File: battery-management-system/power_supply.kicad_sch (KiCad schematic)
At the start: 21 parts, among them U1 L6982C33DR, U2 L6982C33DR

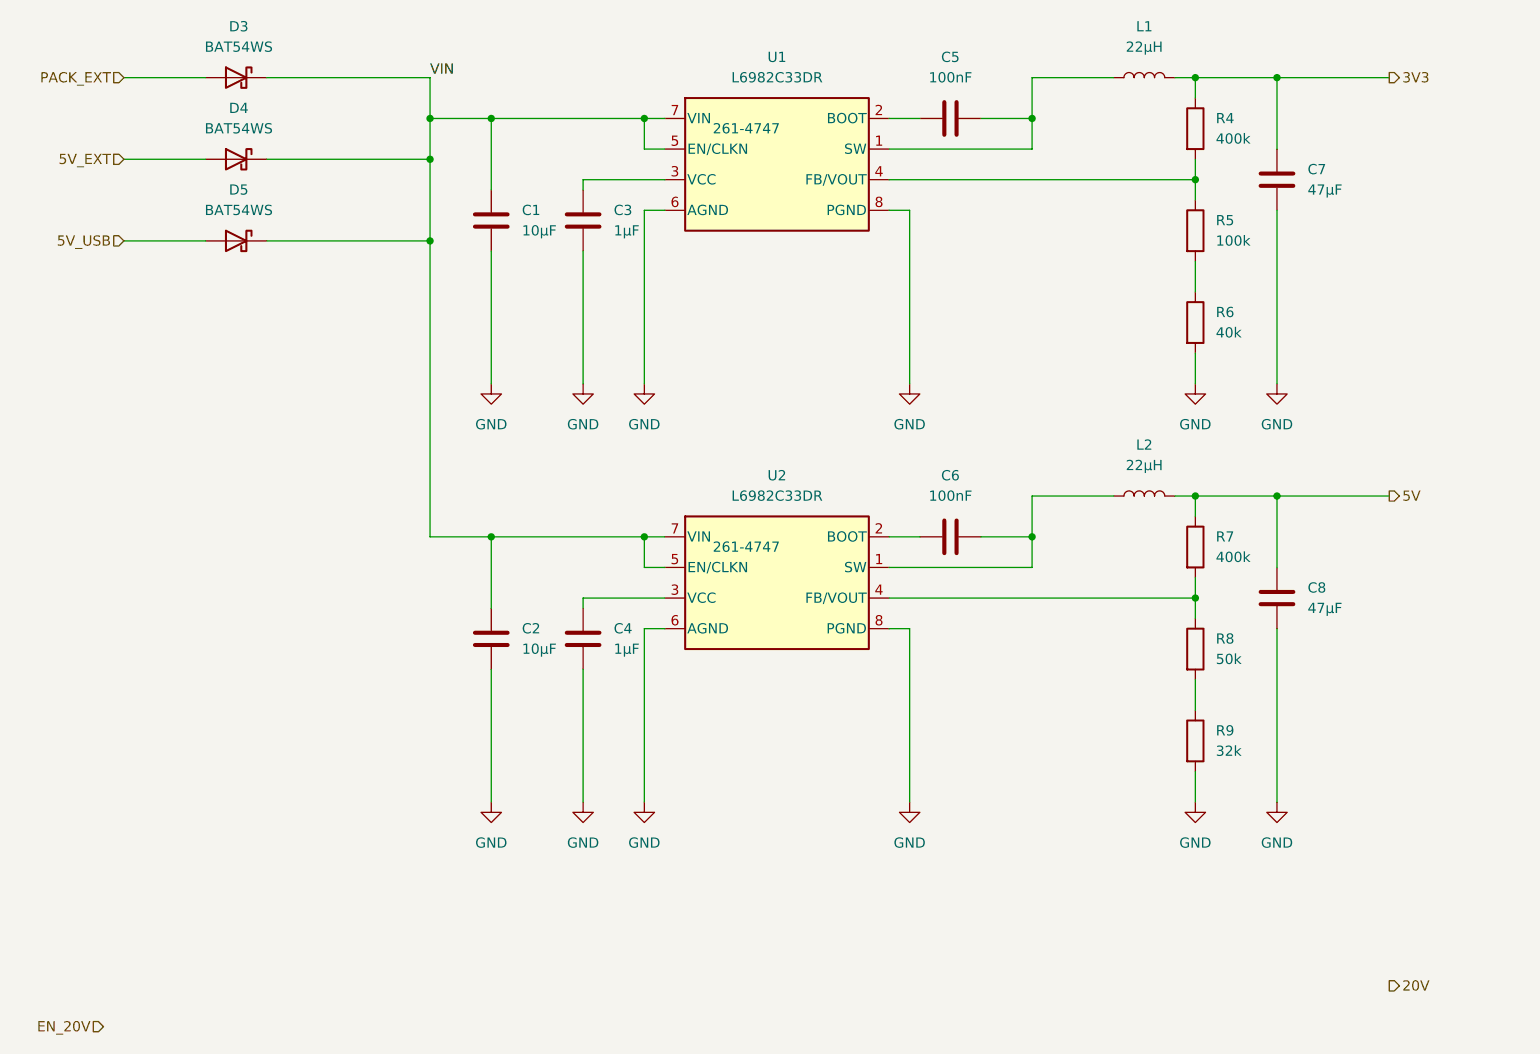
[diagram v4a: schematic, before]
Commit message: specify footprints for resistors, capacitors and inductances
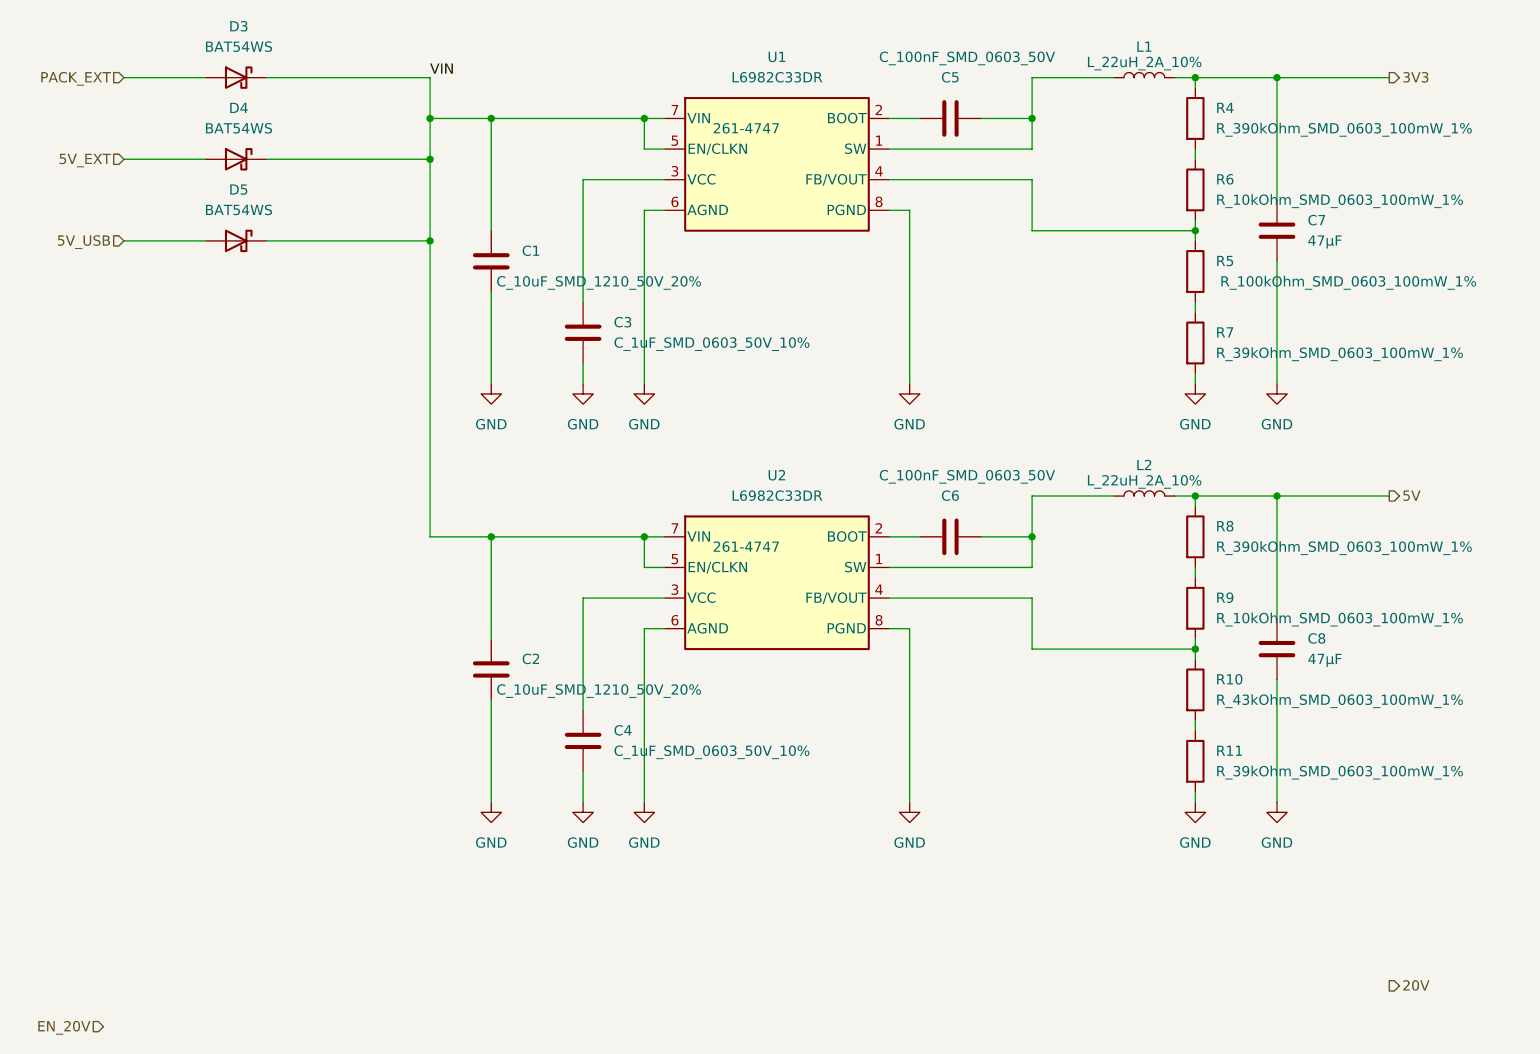
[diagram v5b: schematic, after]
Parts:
- removed C4: 1µF, symbol Device:C
- removed R4, R7: 400k, symbol Device:R
- removed R6: 40k, symbol Device:R
- removed R8: 50k, symbol Device:R
- removed R9: 32k, symbol Device:R
- added C4: C_1uF_SMD_0603_50V_10%, benediktibk:C_0603_1608Metric_Pad1.08x0.95mm_HandSolder, symbol benediktibk:C_1uF_SMD_0603_50V_10%
- added R10: R_43kOhm_SMD_0603_100mW_1%, benediktibk:R_0603_1608Metric_Pad0.98x0.95mm_HandSolder, symbol benediktibk:R_43kOhm_SMD_0603_100mW_1%
- added R11, R7: R_39kOhm_SMD_0603_100mW_1%, benediktibk:R_0603_1608Metric_Pad0.98x0.95mm_HandSolder, symbol benediktibk:R_39kOhm_SMD_0603_100mW_1%
- added R4, R8: R_390kOhm_SMD_0603_100mW_1%, benediktibk:R_0603_1608Metric_Pad0.98x0.95mm_HandSolder, symbol benediktibk:R_390kOhm_SMD_0603_100mW_1%
- added R6, R9: R_10kOhm_SMD_0603_100mW_1%, benediktibk:R_0603_1608Metric_Pad0.98x0.95mm_HandSolder, symbol benediktibk:R_10kOhm_SMD_0603_100mW_1%
- C1, C2: value 10µF -> C_10uF_SMD_1210_50V_20%; footprint (none) -> benediktibk:C_1210_3225Metric_Pad1.33x2.70mm_HandSolder; symbol Device:C -> benediktibk:C_10uF_SMD_1210_50V_20%; RS order number (none) -> 172-1575
- C3: value 1µF -> C_1uF_SMD_0603_50V_10%; footprint (none) -> benediktibk:C_0603_1608Metric_Pad1.08x0.95mm_HandSolder; symbol Device:C -> benediktibk:C_1uF_SMD_0603_50V_10%; RS order number (none) -> 103-4112
- C5, C6: value 100nF -> C_100nF_SMD_0603_50V; footprint (none) -> benediktibk:C_0603_1608Metric_Pad1.08x0.95mm_HandSolder; symbol Device:C -> benediktibk:C_100nF_SMD_0603_50V; RS order number (none) -> 242-7372
- L1, L2: value 22µH -> L_22uH_2A_10%; footprint (none) -> benediktibk:L_Radial_D9.5mm_P5.00mm_Fastron_07HVP; symbol Device:L -> benediktibk:L_22uH_2A_10%; RS order number (none) -> 800-4388
- R5: value 100k -> R_100kOhm_SMD_0603_100mW_1%; footprint (none) -> benediktibk:R_0603_1608Metric_Pad0.98x0.95mm_HandSolder; symbol Device:R -> benediktibk:R_100kOhm_SMD_0603_100mW_1%; RS order number (none) -> 213-2531
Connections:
- net 3V3: now also R4.1
- net 5V: now also R8.1
- net GND: now also C4.2, R11.2, R7.2
- net at R5.1, U1.4 (FB/VOUT): now also R6.2
- net at U2.3 (VCC): now also C4.1
- net at R5.2: now also R7.1
- net at U2.4 (FB/VOUT): now also R10.1, R9.2
- new net: R8.2, R9.1
- new net: R4.2, R6.1
- new net: R10.2, R11.1
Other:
- moved on the sheet: C1, C2, C3, C7, C8, R5

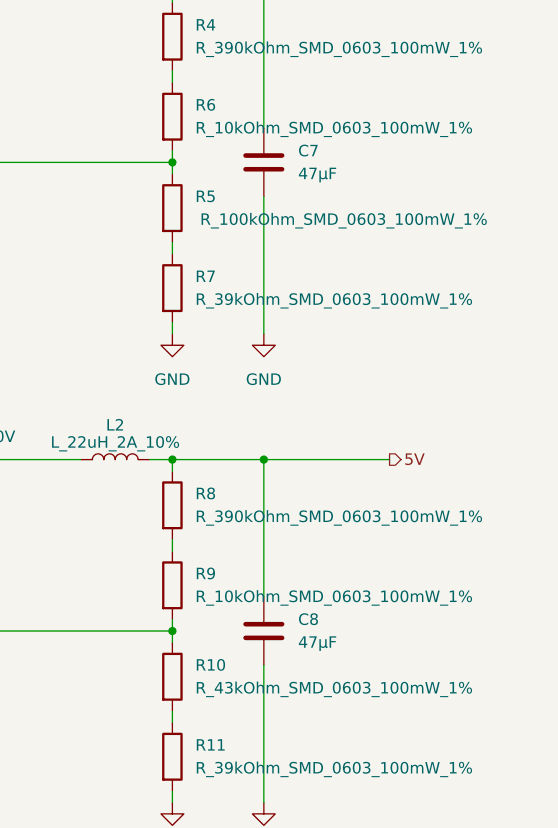
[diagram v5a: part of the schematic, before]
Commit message: specify footprint for 47uF capacitor
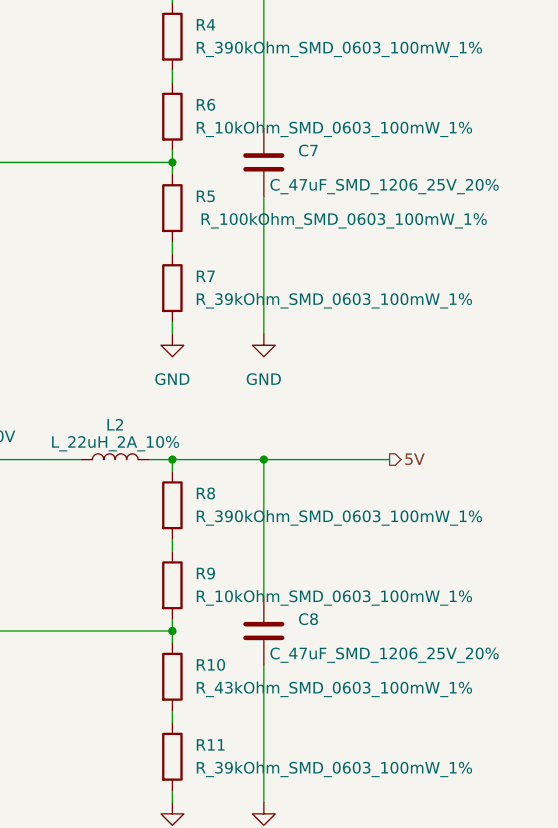
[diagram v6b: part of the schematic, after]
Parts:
- C7, C8: value 47µF -> C_47uF_SMD_1206_25V_20%; footprint (none) -> benediktibk:C_1206_3216Metric_Pad1.33x1.80mm_HandSolder; symbol Device:C -> benediktibk:C_47uF_SMD_1206_25V_20%; RS order number (none) -> 788-3060
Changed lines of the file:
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@@
     (pin "1")
   )
-  (symbol (lib_id "Device:C") (at 172.72 39.37 0) (unit 1)
+  (symbol (lib_id "benediktibk:C_47uF_SMD_1206_25V_20%") (at 172.72 39.37 0) (unit 1)
     (in_bom yes) (on_board yes) (fields_autoplaced)
     (property "Reference" "C7" (id 0) (at 176.53 38.0999 0)
       (effects (font (size 1.27 1.27)) (justify left))
     )
-    (property "Value" "47µF" (id 1) (at 176.53 40.6399 0)
-      (effects (font (size 1.27 1.27)) (justify left))
-    )
-    (property "Footprint" "" (id 2) (at 173.6852 43.18 0)
+    (property "Value" "C_47uF_SMD_1206_25V_20%" (id 1) (at 173.355 41.91 0)
+      (effects (font (size 1.27 1.27)) (justify left))
+    )
+    (property "Footprint" "benediktibk:C_1206_3216Metric_Pad1.33x1.80mm_HandSolder" (id 2) (at 173.6852 43.18 0)
       (effects (font (size 1.27 1.27)) hide)
     )
     (property "Datasheet" "~" (id 3) (at 172.72 39.37 0)
+      (effects (font (size 1.27 1.27)) hide)
+    )
+    (property "RS order number" "788-3060" (id 4) (at 190.246 38.1 0)
       (effects (font (size 1.27 1.27)) hide)
     )
@@
     (pin "1")
   )
-  (symbol (lib_id "Device:C") (at 172.72 91.44 0) (unit 1)
+  (symbol (lib_id "benediktibk:C_47uF_SMD_1206_25V_20%") (at 172.72 91.44 0) (unit 1)
     (in_bom yes) (on_board yes) (fields_autoplaced)
     (property "Reference" "C8" (id 0) (at 176.53 90.1699 0)
       (effects (font (size 1.27 1.27)) (justify left))
     )
-    (property "Value" "47µF" (id 1) (at 176.53 92.7099 0)
-      (effects (font (size 1.27 1.27)) (justify left))
-    )
-    (property "Footprint" "" (id 2) (at 173.6852 95.25 0)
+    (property "Value" "C_47uF_SMD_1206_25V_20%" (id 1) (at 173.355 93.98 0)
+      (effects (font (size 1.27 1.27)) (justify left))
+    )
+    (property "Footprint" "benediktibk:C_1206_3216Metric_Pad1.33x1.80mm_HandSolder" (id 2) (at 173.6852 95.25 0)
       (effects (font (size 1.27 1.27)) hide)
     )
@@
       (effects (font (size 1.27 1.27)) hide)
     )
+    (property "RS order number" "788-3060" (id 4) (at 190.246 90.17 0)
+      (effects (font (size 1.27 1.27)) hide)
+    )
